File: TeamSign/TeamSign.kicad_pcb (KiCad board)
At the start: 2 copper layers, 240 x 145 mm, 215 parts, among them J1 RJ45, J2 Barrel_Jack_MountingPin, Q1 BSS138, Q2 BSS138, U1 TPS563200, U2 ESP32-Devkit_C_V4

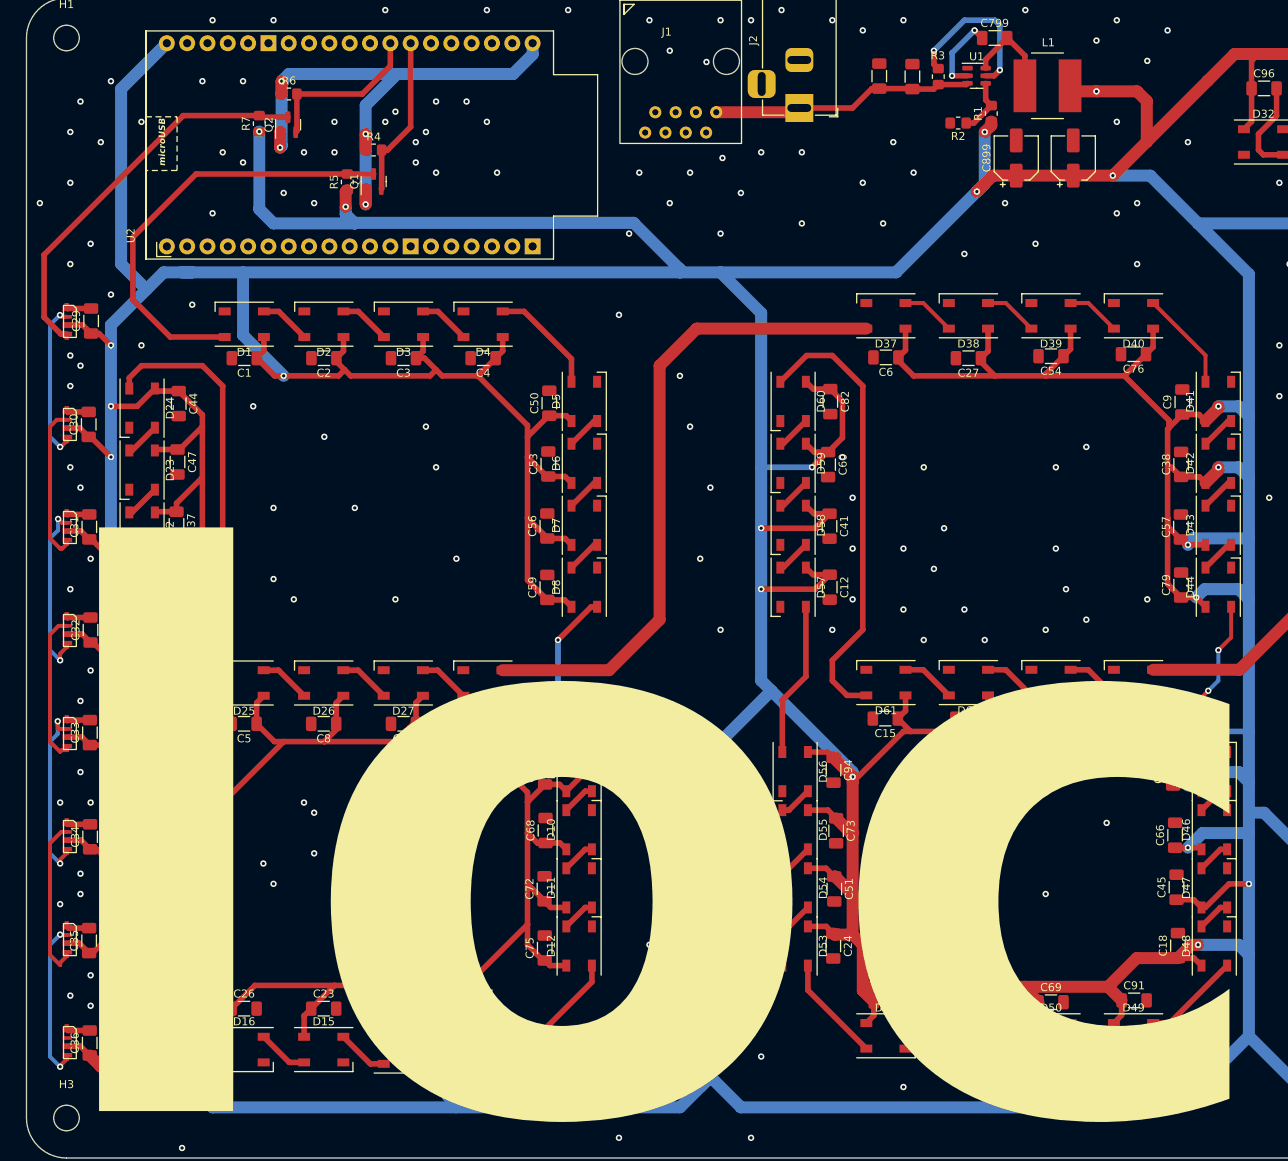
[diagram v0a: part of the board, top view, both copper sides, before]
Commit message: Update BOM + team sign PCB to not have diffuser issue.
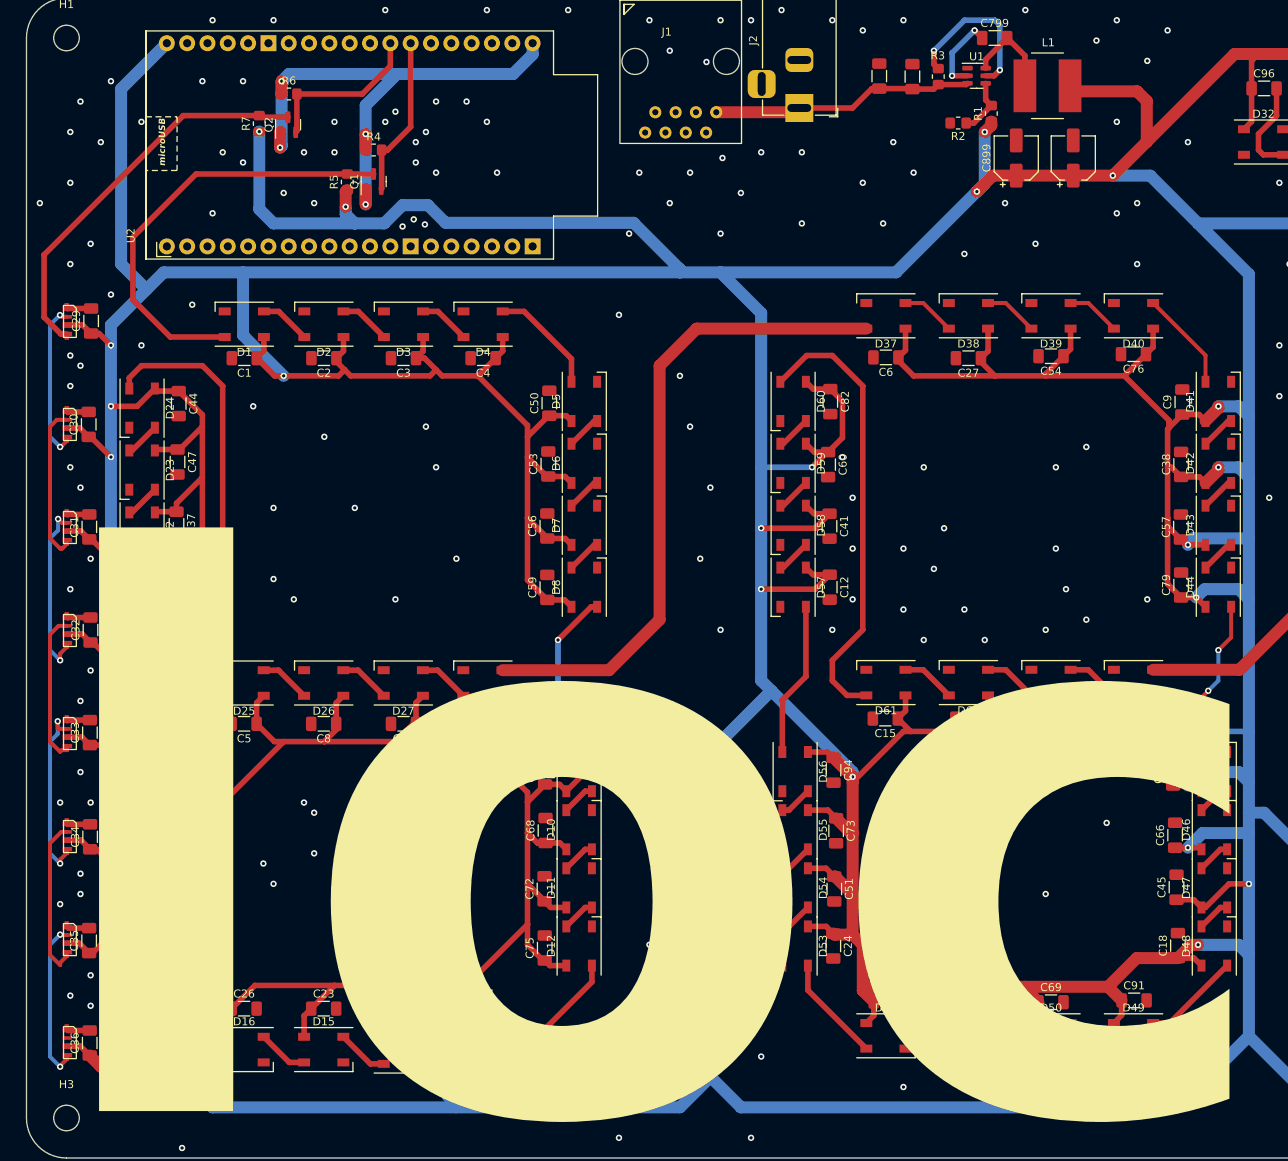
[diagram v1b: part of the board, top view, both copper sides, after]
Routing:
- net +5V: track 2612.7 -> 2611.4 mm, vias 45 -> 43
- net +12V: track 32.9 -> 32.1 mm
- net GND: vias 230 -> 233
